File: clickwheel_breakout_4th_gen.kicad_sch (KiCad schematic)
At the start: 8 parts, among them J1 SFV8R-2STE1HLF, J2 SFV14R-2STE1HLF, J3 SFV8R-2STE1HLF, J4 SFV14R-2STE1HLF, J5 Conn_02x08_Odd_Even, J6 Conn_02x14_Odd_Even, J7 USB_C_Receptacle_USB2.0

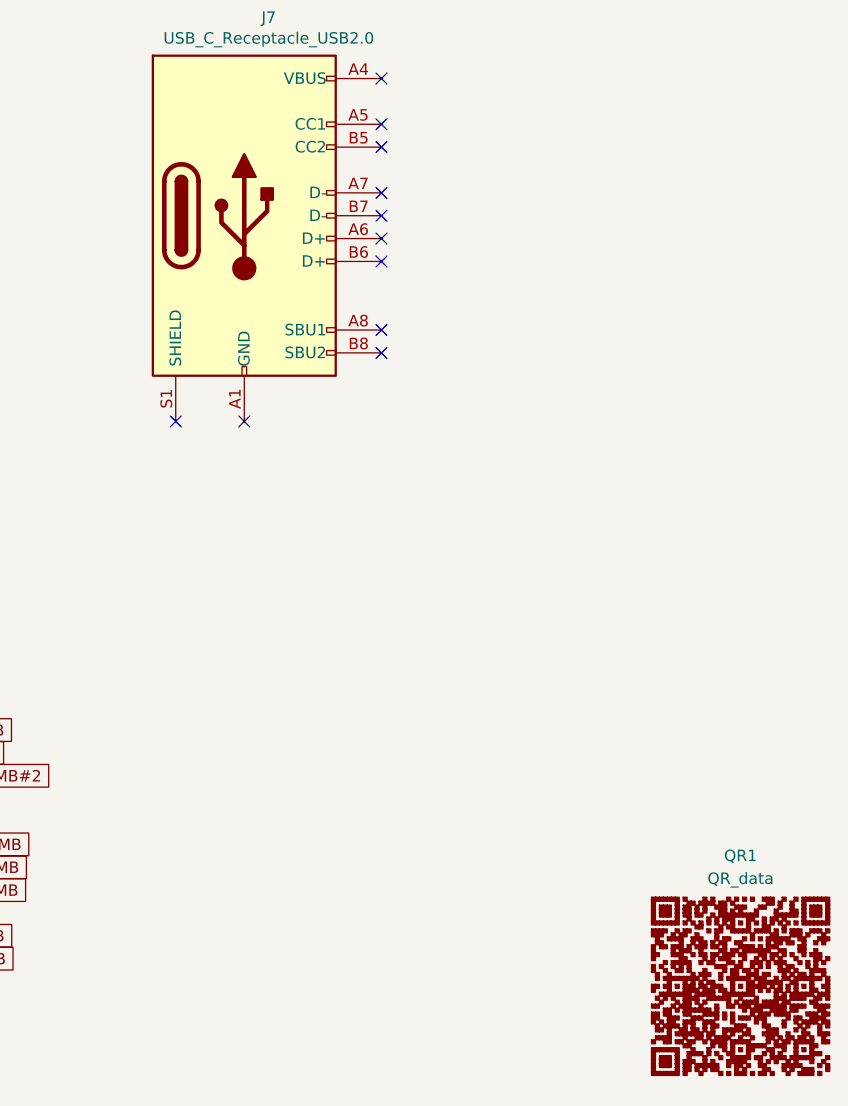
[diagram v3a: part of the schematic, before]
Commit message: project: update to kicad 7, remove qr code
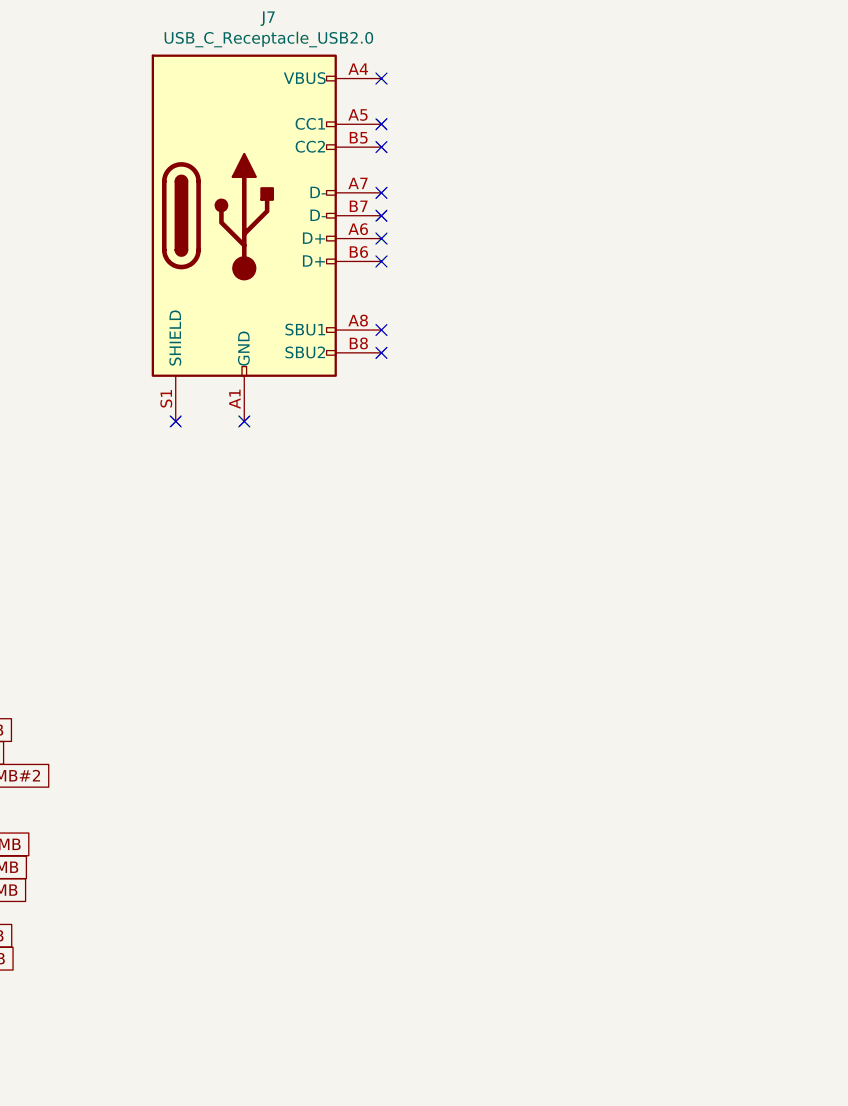
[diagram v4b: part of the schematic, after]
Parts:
- removed QR1: QR_data, QR:QR_data, symbol QR:QR_data

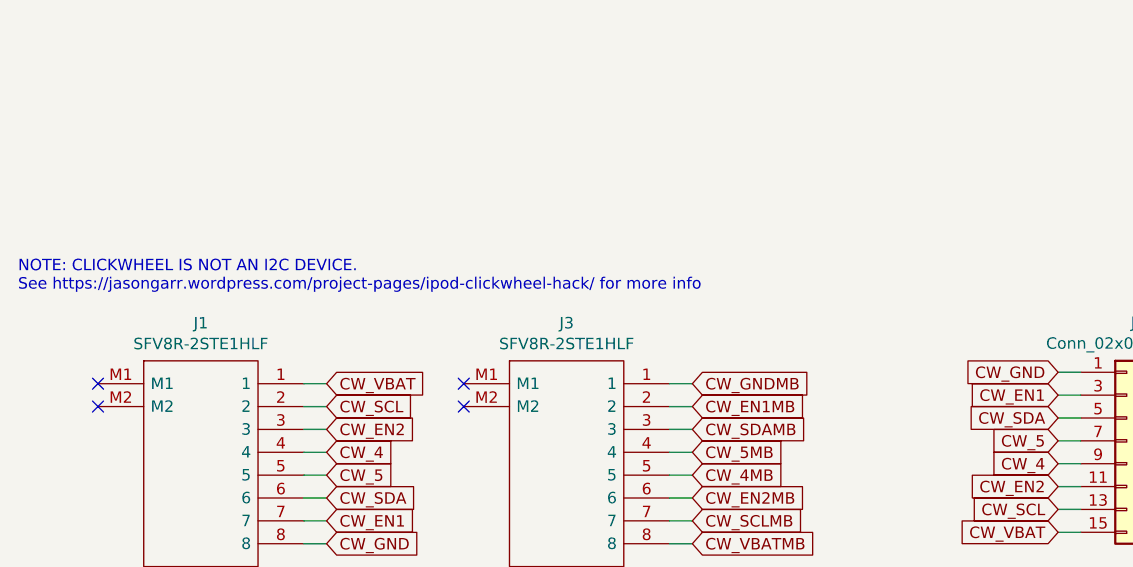
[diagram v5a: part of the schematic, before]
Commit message: info: update link to reverse engineering efforts
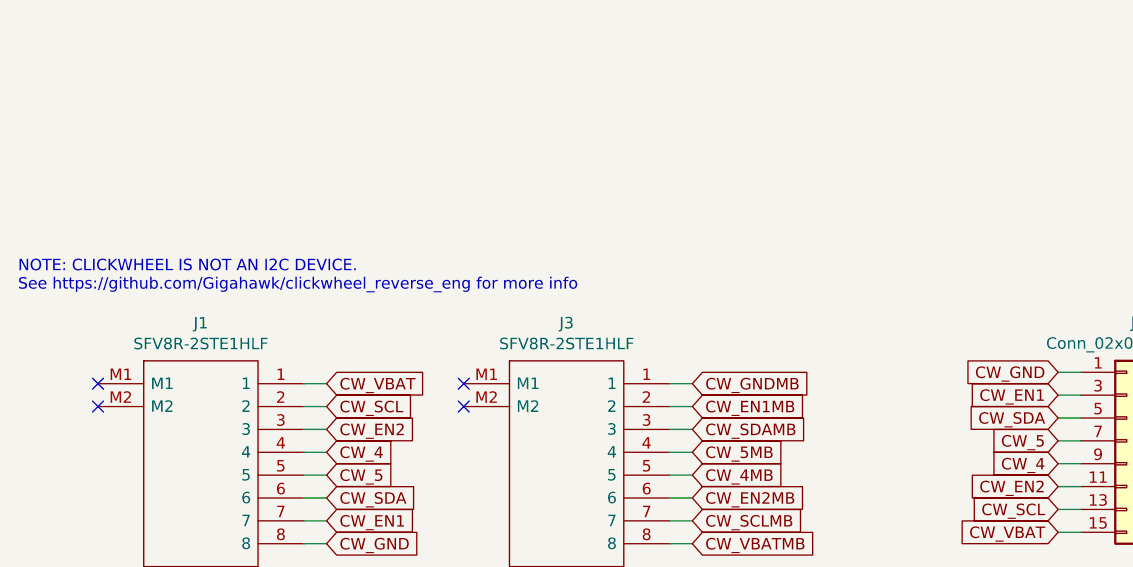
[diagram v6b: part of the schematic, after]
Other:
- note added: "NOTE: CLICKWHEEL IS NOT AN I2C DEVICE. See https://github.com/Gigahawk/clickwheel_reverse_eng for more info"
- note removed: "NOTE: CLICKWHEEL IS NOT AN I2C DEVICE. See https://jasongarr.wordpress.com/project-pages/ipod-clickwheel-hack/ for more info"
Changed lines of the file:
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@@
     (stroke (width 0) (type default))
   )
-  (text "NOTE: CLICKWHEEL IS NOT AN I2C DEVICE.\nSee https://jasongarr.wordpress.com/project-pages/ipod-clickwheel-hack/ for more info"
+  (text "NOTE: CLICKWHEEL IS NOT AN I2C DEVICE.\nSee https://github.com/Gigahawk/clickwheel_reverse_eng for more info"
     (at 29.21 67.31 0)
     (effects (font (size 1.27 1.27)) (justify left bottom))

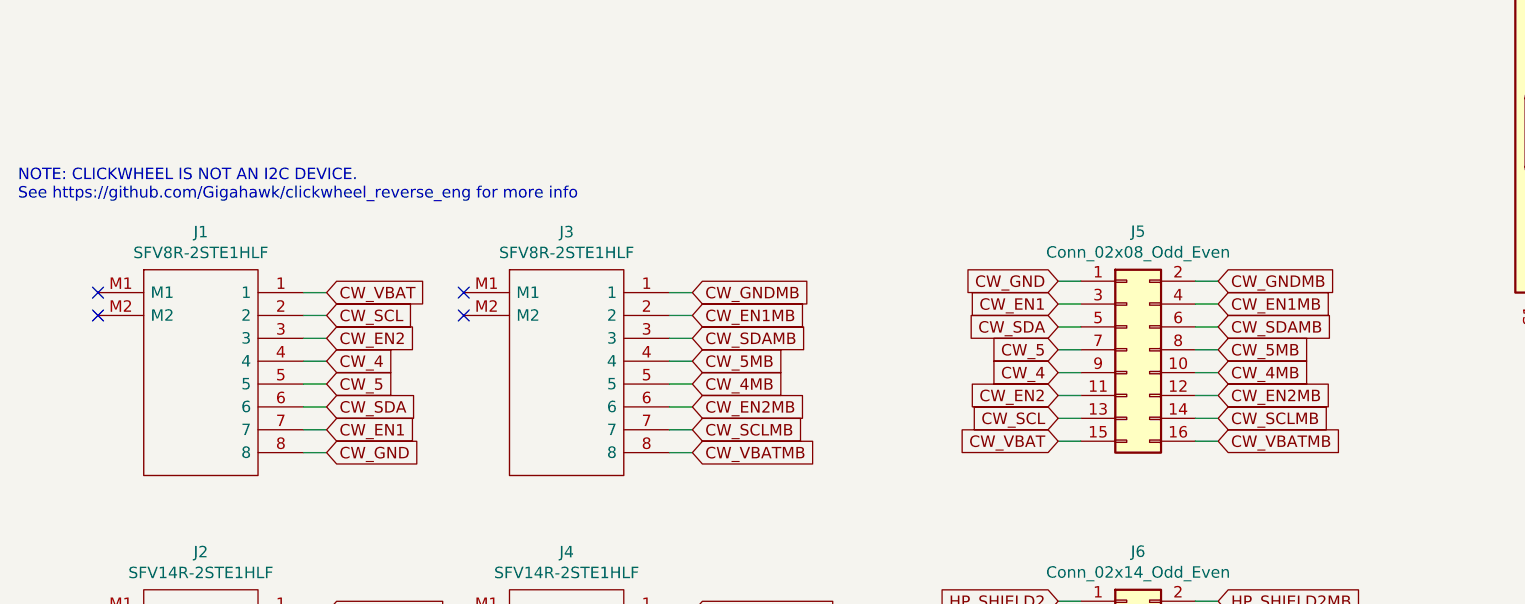
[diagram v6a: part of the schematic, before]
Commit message: schem: update pin names
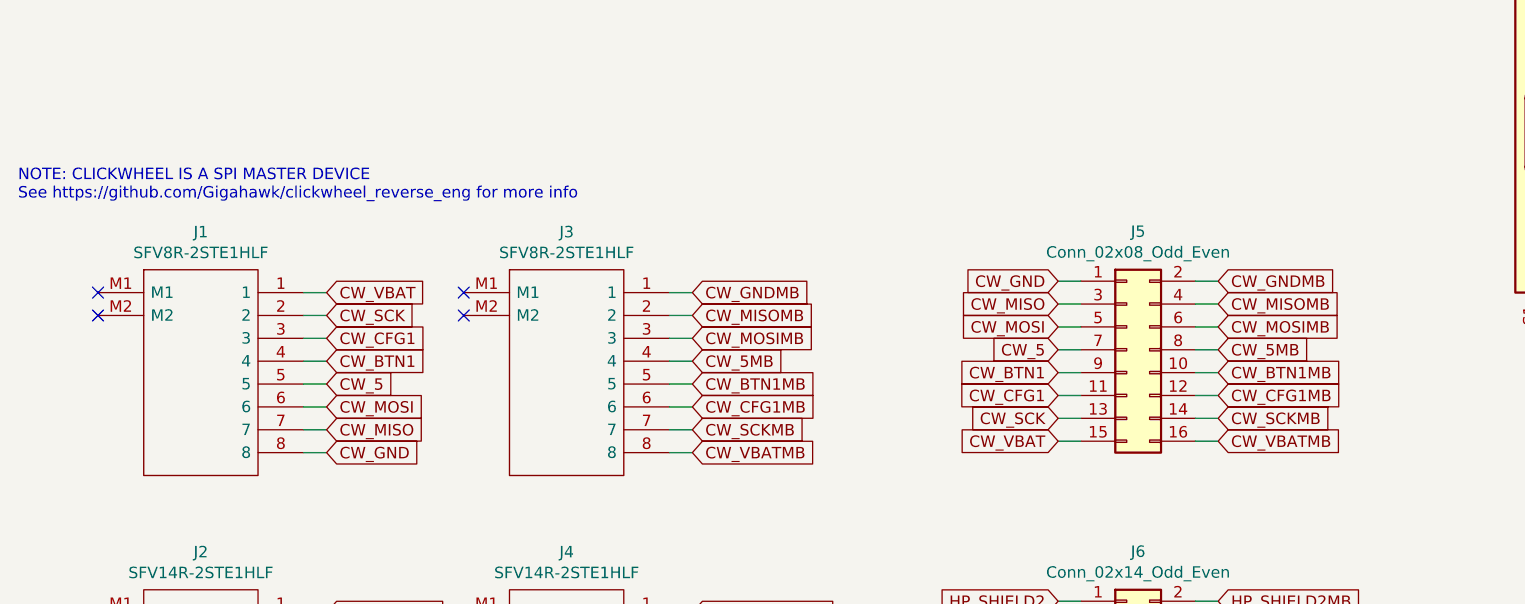
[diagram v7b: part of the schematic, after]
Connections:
- net CW_4 renamed CW_BTN1
- net CW_4MB renamed CW_BTN1MB
- net CW_EN1 renamed CW_MISO
- net CW_EN1MB renamed CW_MISOMB
- net CW_EN2 renamed CW_CFG1
- net CW_EN2MB renamed CW_CFG1MB
- net CW_SCL renamed CW_SCK
- net CW_SCLMB renamed CW_SCKMB
- net CW_SDA renamed CW_MOSI
- net CW_SDAMB renamed CW_MOSIMB
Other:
- note added: "NOTE: CLICKWHEEL IS A SPI MASTER DEVICE See https://github.com/Gigahawk/clickwheel_reverse_eng for more info"
- note removed: "NOTE: CLICKWHEEL IS NOT AN I2C DEVICE. See https://github.com/Gigahawk/clickwheel_reverse_eng for more info"
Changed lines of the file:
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@@
     (stroke (width 0) (type default))
   )
-  (text "NOTE: CLICKWHEEL IS NOT AN I2C DEVICE.\nSee https://github.com/Gigahawk/clickwheel_reverse_eng for more info"
+  (text "NOTE: CLICKWHEEL IS A SPI MASTER DEVICE\nSee https://github.com/Gigahawk/clickwheel_reverse_eng for more info"
     (at 29.21 67.31 0)
     (effects (font (size 1.27 1.27)) (justify left bottom))
@@
     )
   )
-  (global_label "CW_EN2" (shape input) (at 144.78 88.9 180) (fields_autoplaced)
+  (global_label "CW_CFG1" (shape input) (at 144.78 88.9 180) (fields_autoplaced)
     (effects (font (size 1.27 1.27)) (justify right))
     (property "Intersheetrefs" "${INTERSHEET_REFS}" (at 135.1504 88.9 0)
@@
     )
   )
-  (global_label "CW_SCL" (shape input) (at 144.78 91.44 180) (fields_autoplaced)
+  (global_label "CW_SCK" (shape input) (at 144.78 91.44 180) (fields_autoplaced)
     (effects (font (size 1.27 1.27)) (justify right))
     (property "Intersheetrefs" "${INTERSHEET_REFS}" (at 135.3318 91.44 0)
@@
     )
   )
-  (global_label "CW_SDA" (shape input) (at 63.5 90.17 0) (fields_autoplaced)
+  (global_label "CW_MOSI" (shape input) (at 63.5 90.17 0) (fields_autoplaced)
     (effects (font (size 1.27 1.27)) (justify left))
     (property "Intersheetrefs" "${INTERSHEET_REFS}" (at 73.0087 90.17 0)
@@
     )
   )
-  (global_label "CW_EN1" (shape input) (at 144.78 78.74 180) (fields_autoplaced)
+  (global_label "CW_MISO" (shape input) (at 144.78 78.74 180) (fields_autoplaced)
     (effects (font (size 1.27 1.27)) (justify right))
     (property "Intersheetrefs" "${INTERSHEET_REFS}" (at 135.1504 78.74 0)
@@
     )
   )
-  (global_label "CW_4MB" (shape input) (at 162.56 86.36 0) (fields_autoplaced)
+  (global_label "CW_BTN1MB" (shape input) (at 162.56 86.36 0) (fields_autoplaced)
     (effects (font (size 1.27 1.27)) (justify left))
     (property "Intersheetrefs" "${INTERSHEET_REFS}" (at 172.4315 86.36 0)
@@
     )
   )
-  (global_label "CW_4" (shape input) (at 63.5 85.09 0) (fields_autoplaced)
+  (global_label "CW_BTN1" (shape input) (at 63.5 85.09 0) (fields_autoplaced)
     (effects (font (size 1.27 1.27)) (justify left))
     (property "Intersheetrefs" "${INTERSHEET_REFS}" (at 70.6501 85.09 0)
@@
     )
   )
-  (global_label "CW_EN2MB" (shape input) (at 162.56 88.9 0) (fields_autoplaced)
+  (global_label "CW_CFG1MB" (shape input) (at 162.56 88.9 0) (fields_autoplaced)
     (effects (font (size 1.27 1.27)) (justify left))
     (property "Intersheetrefs" "${INTERSHEET_REFS}" (at 174.911 88.9 0)
@@
     )
   )
-  (global_label "CW_SDAMB" (shape input) (at 104.14 82.55 0) (fields_autoplaced)
+  (global_label "CW_MOSIMB" (shape input) (at 104.14 82.55 0) (fields_autoplaced)
     (effects (font (size 1.27 1.27)) (justify left))
     (property "Intersheetrefs" "${INTERSHEET_REFS}" (at 116.3701 82.55 0)
@@
     )
   )
-  (global_label "CW_EN1MB" (shape input) (at 162.56 78.74 0) (fields_autoplaced)
+  (global_label "CW_MISOMB" (shape input) (at 162.56 78.74 0) (fields_autoplaced)
     (effects (font (size 1.27 1.27)) (justify left))
     (property "Intersheetrefs" "${INTERSHEET_REFS}" (at 174.911 78.74 0)
@@
     )
   )
-  (global_label "CW_SDA" (shape input) (at 144.78 81.28 180) (fields_autoplaced)
+  (global_label "CW_MOSI" (shape input) (at 144.78 81.28 180) (fields_autoplaced)
     (effects (font (size 1.27 1.27)) (justify right))
     (property "Intersheetrefs" "${INTERSHEET_REFS}" (at 135.2713 81.28 0)
@@
     )
   )
-  (global_label "CW_EN1MB" (shape input) (at 104.14 80.01 0) (fields_autoplaced)
+  (global_label "CW_MISOMB" (shape input) (at 104.14 80.01 0) (fields_autoplaced)
     (effects (font (size 1.27 1.27)) (justify left))
     (property "Intersheetrefs" "${INTERSHEET_REFS}" (at 116.491 80.01 0)
@@
     )
   )
-  (global_label "CW_4MB" (shape input) (at 104.14 87.63 0) (fields_autoplaced)
+  (global_label "CW_BTN1MB" (shape input) (at 104.14 87.63 0) (fields_autoplaced)
     (effects (font (size 1.27 1.27)) (justify left))
     (property "Intersheetrefs" "${INTERSHEET_REFS}" (at 114.0115 87.63 0)
@@
     )
   )
-  (global_label "CW_SDAMB" (shape input) (at 162.56 81.28 0) (fields_autoplaced)
+  (global_label "CW_MOSIMB" (shape input) (at 162.56 81.28 0) (fields_autoplaced)
     (effects (font (size 1.27 1.27)) (justify left))
     (property "Intersheetrefs" "${INTERSHEET_REFS}" (at 174.7901 81.28 0)
@@
     )
   )
-  (global_label "CW_SCL" (shape input) (at 63.5 80.01 0) (fields_autoplaced)
+  (global_label "CW_SCK" (shape input) (at 63.5 80.01 0) (fields_autoplaced)
     (effects (font (size 1.27 1.27)) (justify left))
     (property "Intersheetrefs" "${INTERSHEET_REFS}" (at 72.9482 80.01 0)
@@
     )
   )
-  (global_label "CW_SCLMB" (shape input) (at 104.14 92.71 0) (fields_autoplaced)
+  (global_label "CW_SCKMB" (shape input) (at 104.14 92.71 0) (fields_autoplaced)
     (effects (font (size 1.27 1.27)) (justify left))
     (property "Intersheetrefs" "${INTERSHEET_REFS}" (at 116.3096 92.71 0)
@@
     )
   )
-  (global_label "CW_EN2" (shape input) (at 63.5 82.55 0) (fields_autoplaced)
+  (global_label "CW_CFG1" (shape input) (at 63.5 82.55 0) (fields_autoplaced)
     (effects (font (size 1.27 1.27)) (justify left))
     (property "Intersheetrefs" "${INTERSHEET_REFS}" (at 73.1296 82.55 0)
@@
     )
   )
-  (global_label "CW_EN2MB" (shape input) (at 104.14 90.17 0) (fields_autoplaced)
+  (global_label "CW_CFG1MB" (shape input) (at 104.14 90.17 0) (fields_autoplaced)
     (effects (font (size 1.27 1.27)) (justify left))
     (property "Intersheetrefs" "${INTERSHEET_REFS}" (at 116.491 90.17 0)
@@
     )
   )
-  (global_label "CW_SCLMB" (shape input) (at 162.56 91.44 0) (fields_autoplaced)
+  (global_label "CW_SCKMB" (shape input) (at 162.56 91.44 0) (fields_autoplaced)
     (effects (font (size 1.27 1.27)) (justify left))
     (property "Intersheetrefs" "${INTERSHEET_REFS}" (at 174.7296 91.44 0)
@@
     )
   )
-  (global_label "CW_4" (shape input) (at 144.78 86.36 180) (fields_autoplaced)
+  (global_label "CW_BTN1" (shape input) (at 144.78 86.36 180) (fields_autoplaced)
     (effects (font (size 1.27 1.27)) (justify right))
     (property "Intersheetrefs" "${INTERSHEET_REFS}" (at 137.6299 86.36 0)
@@
     )
   )
-  (global_label "CW_EN1" (shape input) (at 63.5 92.71 0) (fields_autoplaced)
+  (global_label "CW_MISO" (shape input) (at 63.5 92.71 0) (fields_autoplaced)
     (effects (font (size 1.27 1.27)) (justify left))
     (property "Intersheetrefs" "${INTERSHEET_REFS}" (at 73.1296 92.71 0)
